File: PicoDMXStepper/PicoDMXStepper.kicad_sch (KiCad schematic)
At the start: 26 parts, among them J1 Pwr In, J2 DMX Serial, J3 Stepper Out, J4 Limit SW, SW2 SW_DIP_x04, U1 AMS1117-5.0, U2 Pico, U3 SP3485EN

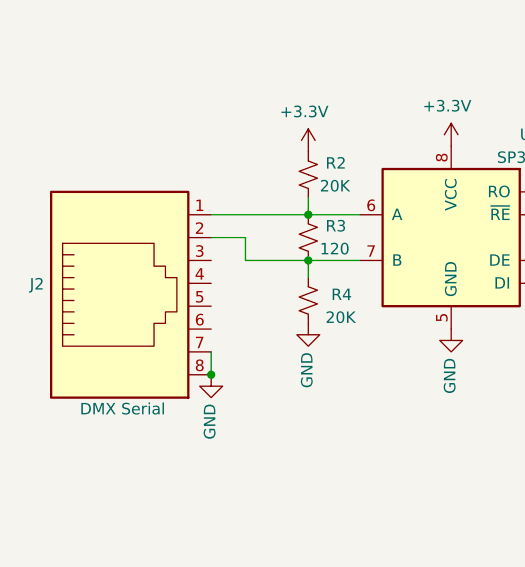
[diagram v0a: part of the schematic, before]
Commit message: Added untested Firmware and LCSC partnumbers
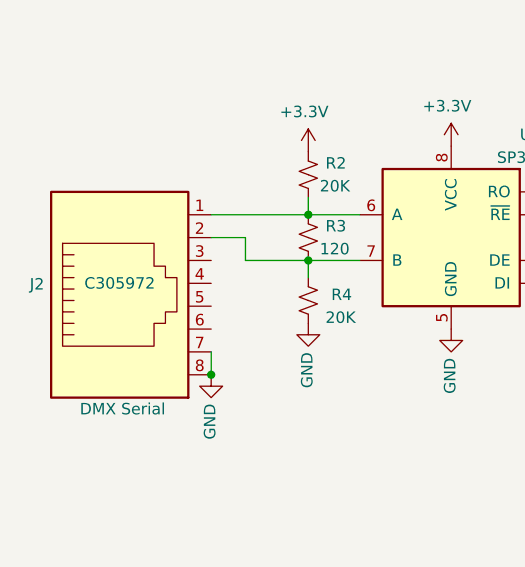
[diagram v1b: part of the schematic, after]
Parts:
- C1: LCSC (none) -> C445063
- C2: LCSC (none) -> C19702
- D1, R3: LCSC (none) -> C72043
- J1: LCSC (none) -> C306200
- J2: LCSC (none) -> C305972
- J3: LCSC (none) -> C192779
- J4: LCSC (none) -> C69809
- R1: LCSC (none) -> C23345
- R2, R4: LCSC (none) -> C4184
- R5, R6: LCSC (none) -> C25804
- SW2: LCSC (none) -> C509571
- U1: LCSC (none) -> C6187
- U3: LCSC (none) -> C8963
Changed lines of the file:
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@@
+      (effects (font (size 1.27 1.27)) hide)
+    )
+    (property "LCSC" "C306200" (at 55.626 49.657 0)
       (effects (font (size 1.27 1.27)) hide)
     )
@@
       (effects (font (size 1.27 1.27)) hide)
     )
+    (property "LCSC" "C445063" (at 80.4672 50.9016 0)
+      (effects (font (size 1.27 1.27)) hide)
+    )
     (pin "1")
     (pin "2")
@@
     )
     (property "Datasheet" "~" (at 104.14 52.07 0)
+      (effects (font (size 1.27 1.27)) hide)
+    )
+    (property "LCSC" "C19702" (at 107.1372 50.9016 0)
       (effects (font (size 1.27 1.27)) hide)
     )
@@
       (effects (font (size 1.27 1.27)) hide)
     )
-    (property "LCSC" "" (at 52.705 102.87 0)
+    (property "LCSC" "C305972" (at 52.705 102.87 0)
       (effects (font (size 1.27 1.27)))
     )
@@
       (effects (font (size 1.27 1.27)) hide)
     )
+    (property "LCSC" "C25804" (at 101.6 104.775 0)
+      (effects (font (size 1.27 1.27)) hide)
+    )
     (pin "1")
     (pin "2")
@@
       (effects (font (size 1.27 1.27)) hide)
     )
+    (property "LCSC" "C72043" (at 140.208 34.036 0)
+      (effects (font (size 1.27 1.27)) hide)
+    )
     (pin "1")
     (pin "2")
@@
     )
     (property "LCSC_PN" "C4184" (at 73.66 104.775 0)
+      (effects (font (size 1.27 1.27)) hide)
+    )
+    (property "LCSC" "C4184" (at 76.2 104.14 0)
       (effects (font (size 1.27 1.27)) hide)
     )
@@
     )
     (property "LCSC_PN" "C6187" (at 91.44 48.26 0)
+      (effects (font (size 1.27 1.27)) hide)
+    )
+    (property "LCSC" "C6187" (at 91.44 41.91 0)
       (effects (font (size 1.27 1.27)) hide)
     )
@@
       (effects (font (size 1.27 1.27)) hide)
     )
+    (property "LCSC" "C509571" (at 141.986 103.124 0)
+      (effects (font (size 1.27 1.27)) hide)
+    )
     (pin "1")
     (pin "2")
@@
       (effects (font (size 1.27 1.27)) hide)
     )
+    (property "LCSC" "C192779" (at 215.646 127.635 0)
+      (effects (font (size 1.27 1.27)) hide)
+    )
     (pin "1")
     (pin "2")
@@
       (effects (font (size 1.27 1.27)) hide)
     )
+    (property "LCSC" "C25804" (at 109.22 102.235 0)
+      (effects (font (size 1.27 1.27)) hide)
+    )
     (pin "1")
     (pin "2")
@@
     )
     (property "LCSC_PN" "C8963" (at 89.535 97.79 0)
+      (effects (font (size 1.27 1.27)) hide)
+    )
+    (property "LCSC" "C8963" (at 97.155 86.36 0)
       (effects (font (size 1.27 1.27)) hide)
     )
@@
       (effects (font (size 1.27 1.27)) hide)
     )
+    (property "LCSC" "C72043" (at 75.565 96.52 0)
+      (effects (font (size 1.27 1.27)) hide)
+    )
     (pin "1")
     (pin "2")
@@
       (effects (font (size 1.27 1.27)) hide)
     )
+    (property "LCSC" "C23345" (at 129.667 42.418 0)
+      (effects (font (size 1.27 1.27)) hide)
+    )
     (pin "1")
     (pin "2")
@@
     )
     (property "LCSC_PN" "C430599" (at 210.566 74.93 0)
+      (effects (font (size 1.27 1.27)) hide)
+    )
+    (property "LCSC" "C69809" (at 212.852 74.295 0)
       (effects (font (size 1.27 1.27)) hide)
     )
@@
       (effects (font (size 1.27 1.27)) hide)
     )
+    (property "LCSC" "C4184" (at 75.565 89.535 0)
+      (effects (font (size 1.27 1.27)) hide)
+    )

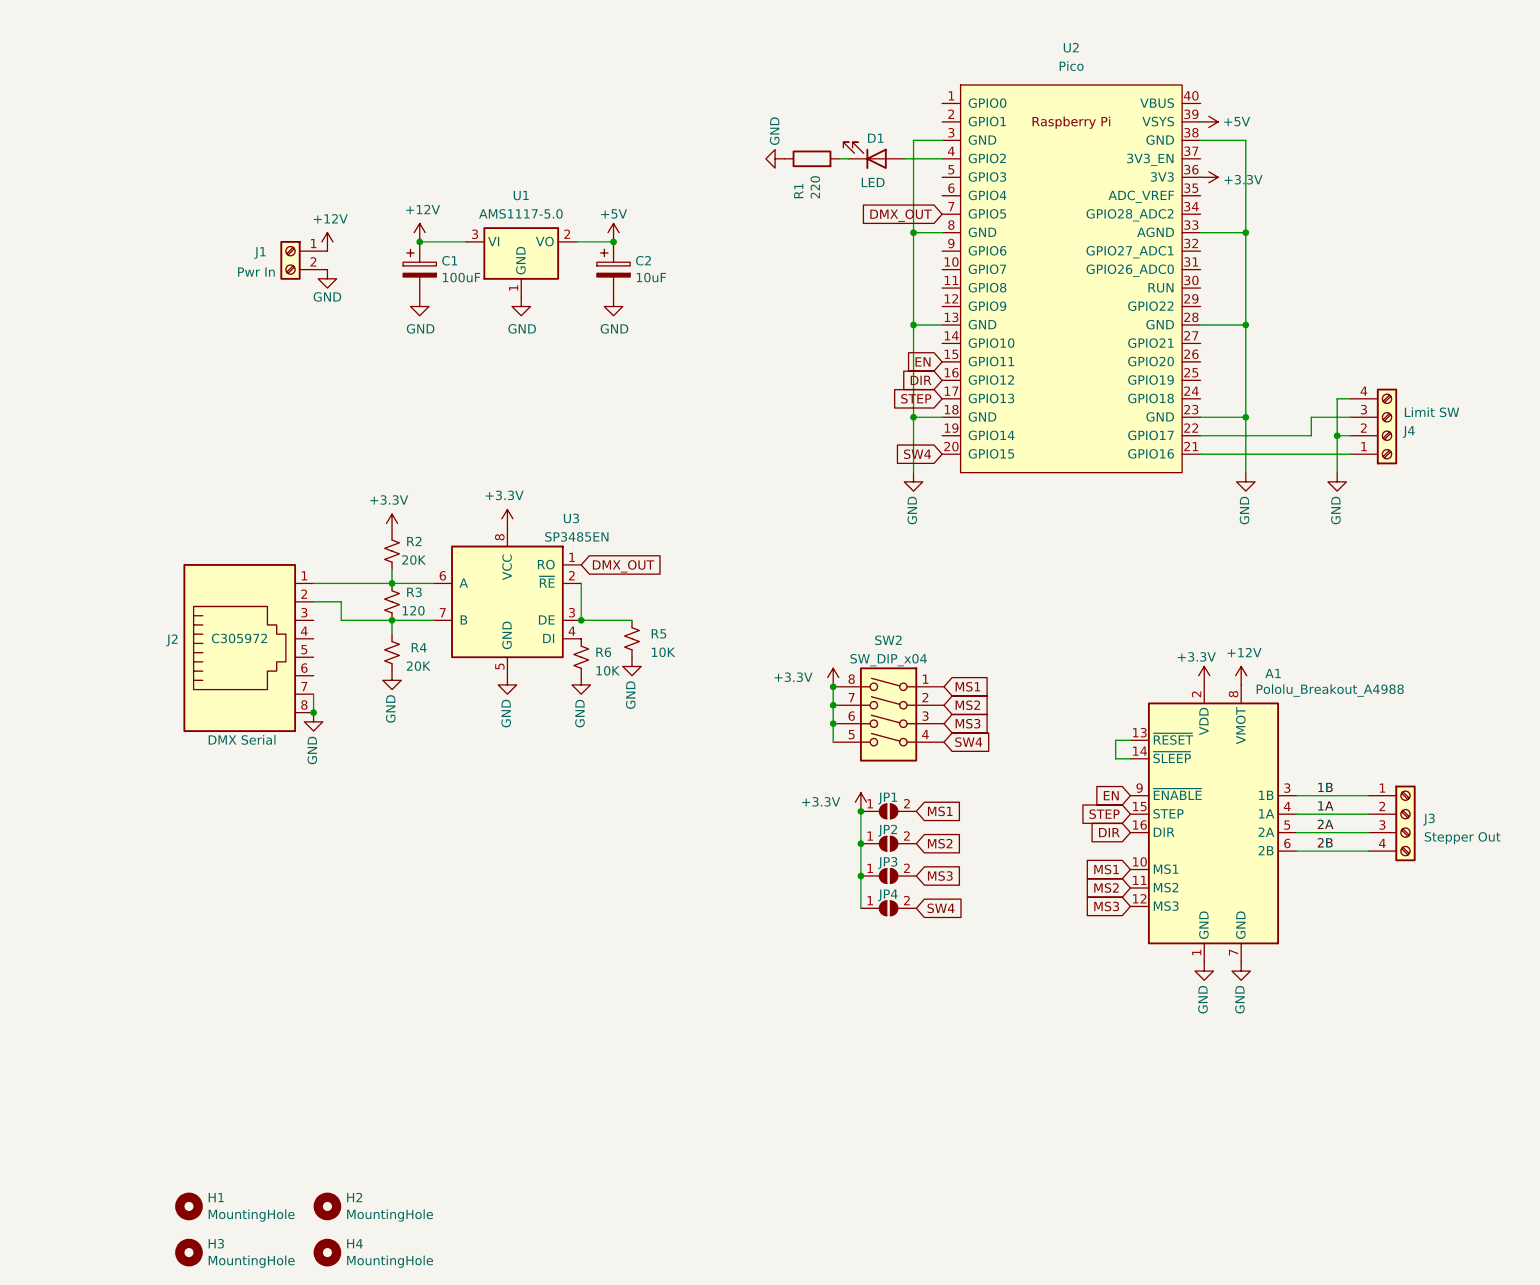
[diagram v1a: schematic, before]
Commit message: redo PCB layout, Add servo headers and opocouplers to limit switches
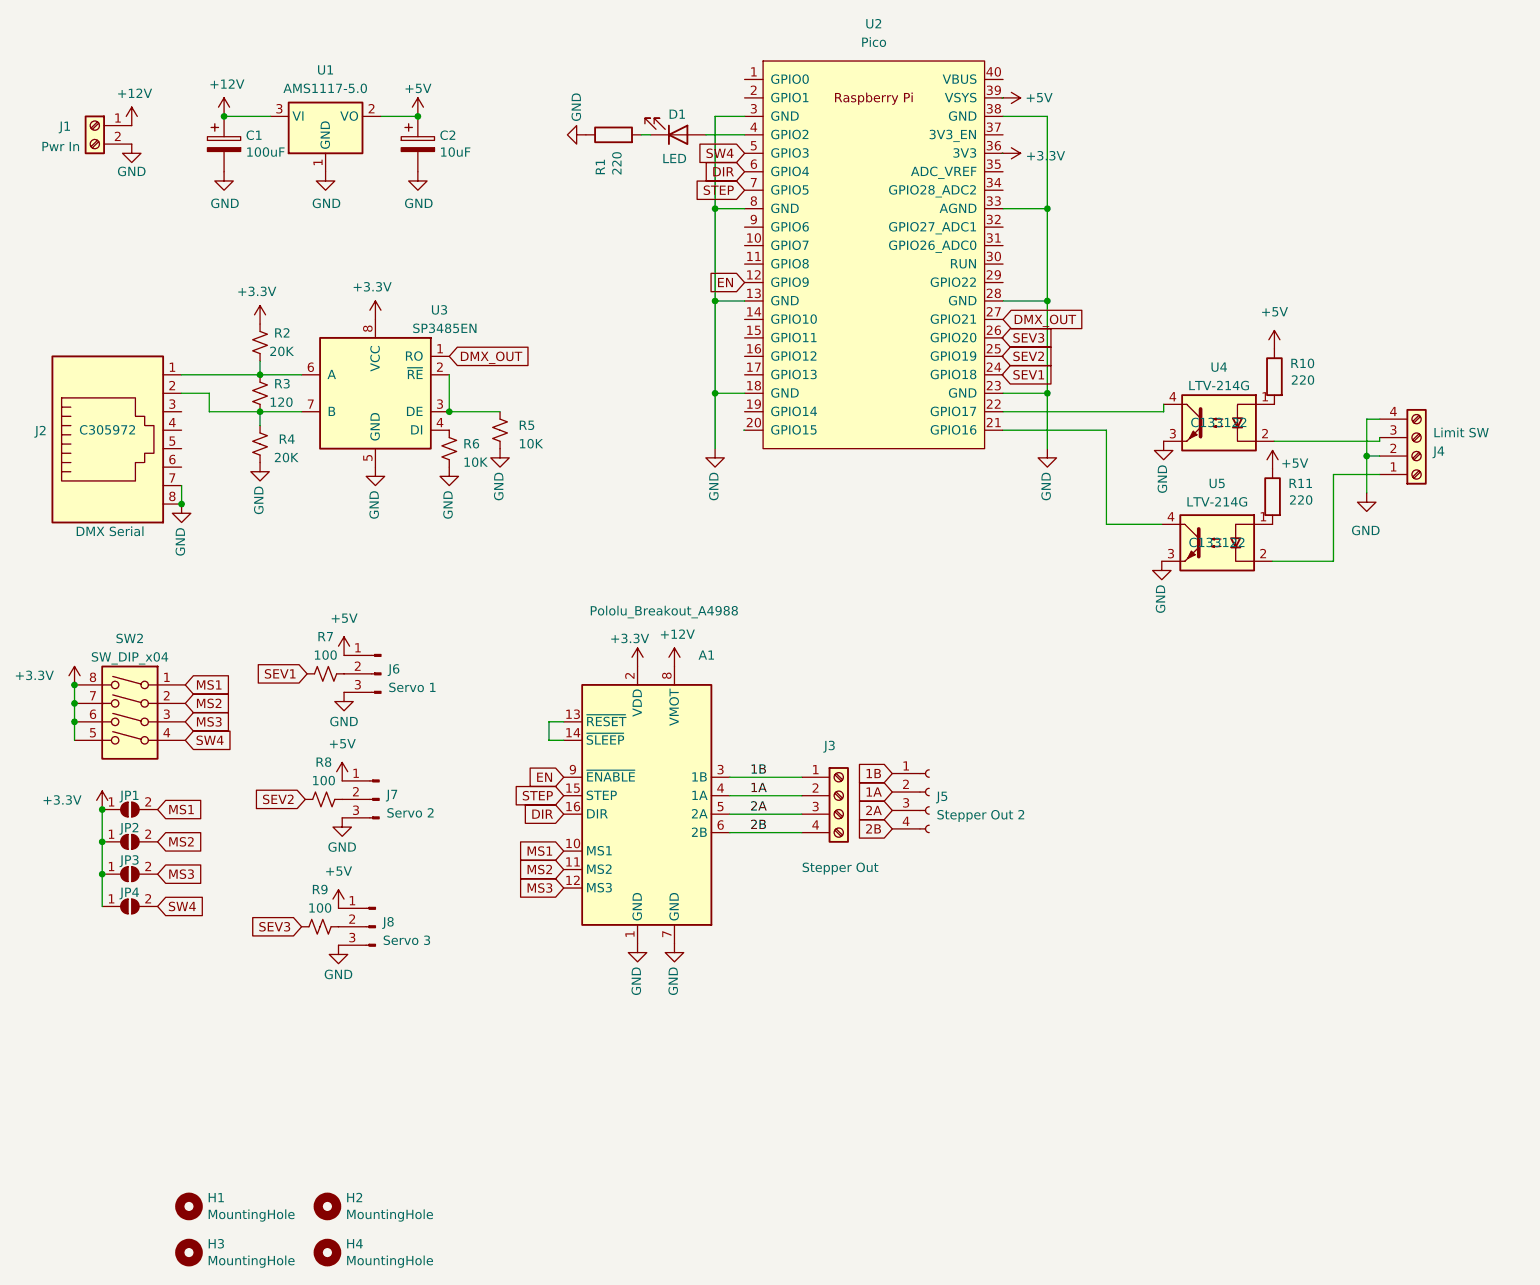
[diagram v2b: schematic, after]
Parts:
- added J5: Stepper Out 2, Connector_JST:JST_XH_B4B-XH-A_1x04_P2.50mm_Vertical, symbol Connector:Conn_01x04_Socket
- added J6: Servo 1, Connector_PinHeader_2.54mm:PinHeader_1x03_P2.54mm_Vertical, symbol Connector:Conn_01x03_Pin
- added J7: Servo 2, Connector_PinHeader_2.54mm:PinHeader_1x03_P2.54mm_Vertical, symbol Connector:Conn_01x03_Pin
- added J8: Servo 3, Connector_PinHeader_2.54mm:PinHeader_1x03_P2.54mm_Vertical, symbol Connector:Conn_01x03_Pin
- added R10, R11: 220, Resistor_SMD:R_0603_1608Metric_Pad0.98x0.95mm_HandSolder, symbol Device:R
- added R7, R8, R9: 100, Resistor_SMD:R_0603_1608Metric_Pad0.98x0.95mm_HandSolder, symbol Device:R_Small_US
- added U4, U5: LTV-214G, PicoDMXStepper:LTV214, symbol LTV-214:LTV-214G
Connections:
- net +5V: now also J6.1 (Pin_1), J7.1 (Pin_1), J8.1 (Pin_1), R10.1, R11.1
- net 1A: now also J5.2 (Pin_2)
- net 1B: now also J5.1 (Pin_1)
- net 2A: now also J5.3 (Pin_3)
- net 2B: now also J5.4 (Pin_4)
- net DIR: now also U2.6 (GPIO4); no longer U2.16 (GPIO12)
- net DMX_OUT: now also U2.27 (GPIO21); no longer U2.7 (GPIO5)
- net EN: now also U2.12 (GPIO9); no longer U2.15 (GPIO11)
- net GND: now also J6.3 (Pin_3), J7.3 (Pin_3), J8.3 (Pin_3), U4.3, U5.3
- net STEP: now also U2.7 (GPIO5); no longer U2.17 (GPIO13)
- net SW4: now also U2.5 (GPIO3); no longer U2.20 (GPIO15)
- net at J4.1 (Pin_1): now also U5.2; no longer U2.21 (GPIO16)
- net at J4.3 (Pin_3): now also U4.2; no longer U2.22 (GPIO17)
- net SEV1: now reaches U2.24 (GPIO18)
- net SEV1: now also R7.1
- net SEV2: now reaches U2.25 (GPIO19)
- net SEV2: now also R8.1
- net SEV3: now reaches U2.26 (GPIO20)
- net SEV3: now also R9.1
- new net: J6.2 (Pin_2), R7.2
- new net: R11.2, U5.1
- new net: U2.21 (GPIO16), U5.4
- new net: R10.2, U4.1
- new net: U2.22 (GPIO17), U4.4
- new net: J8.2 (Pin_2), R9.2
- new net: J7.2 (Pin_2), R8.2
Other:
- moved on the sheet: A1, C1, C2, D1, J1, J2, J3, J4, JP1, JP2, JP3, JP4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

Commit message: added Optocoupler to limits switches
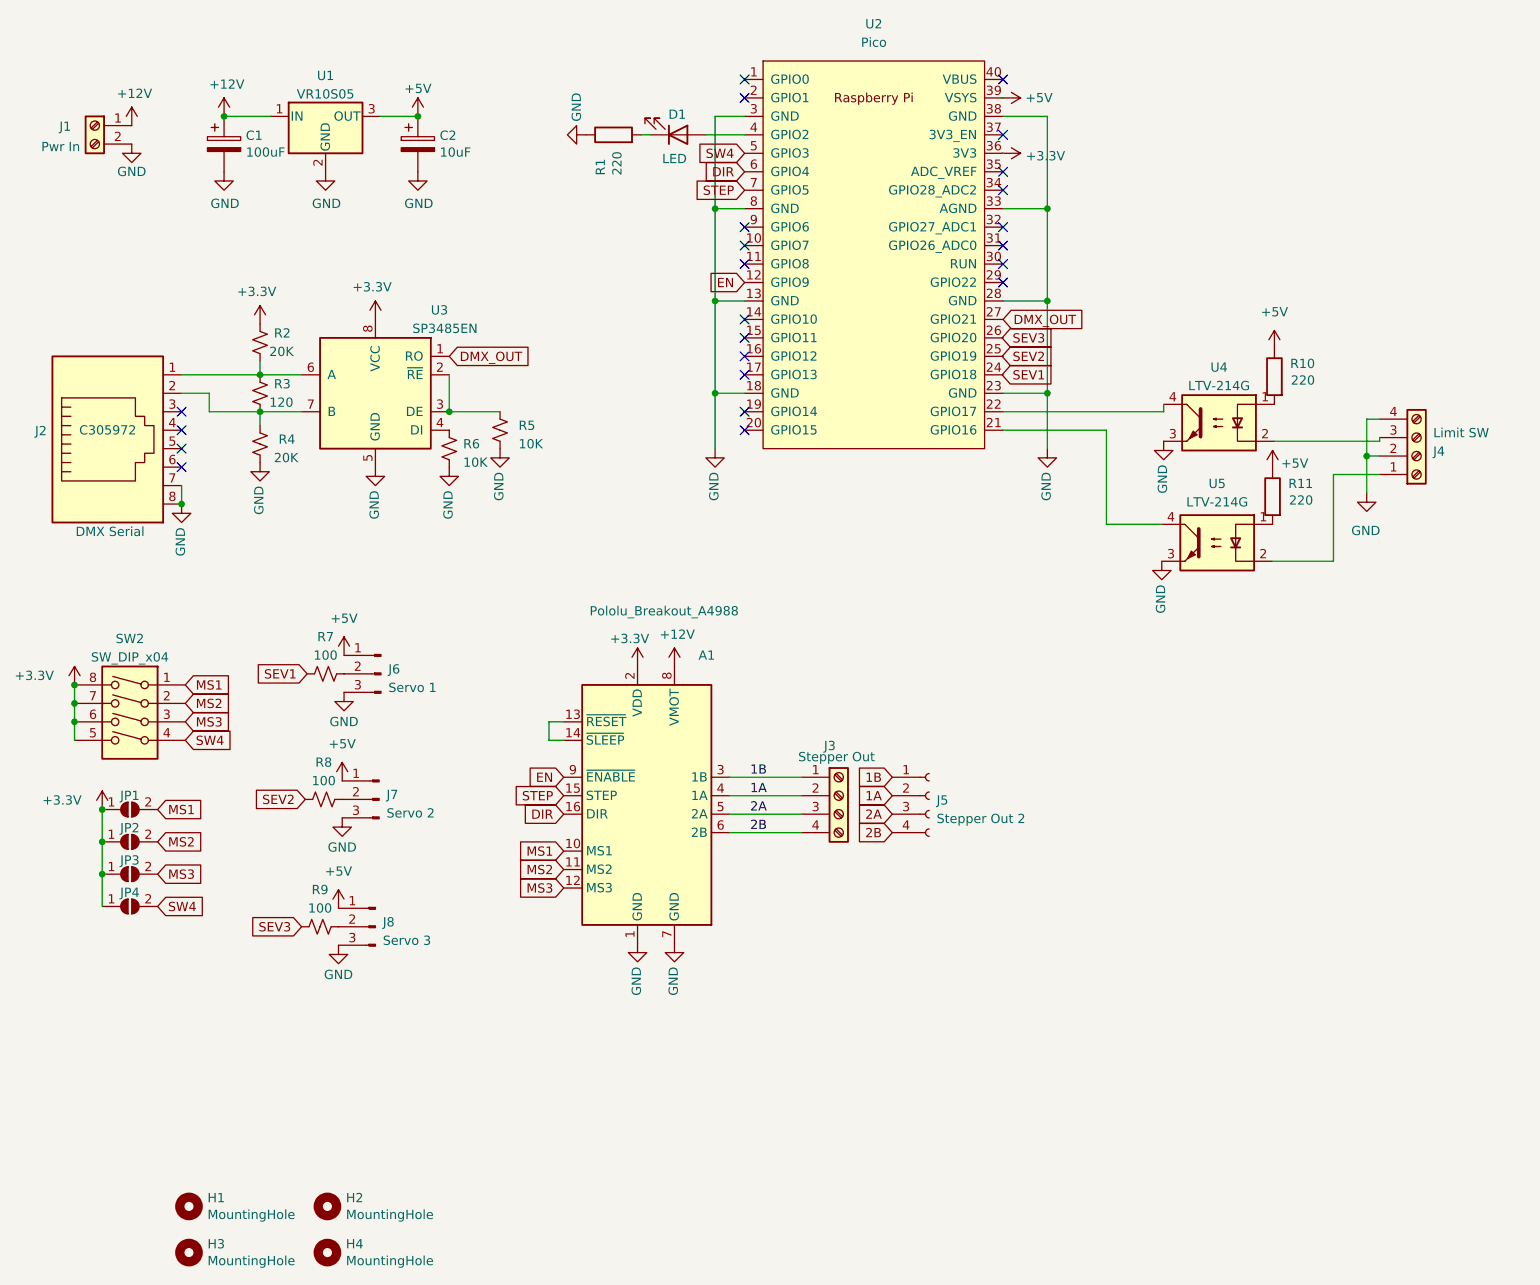
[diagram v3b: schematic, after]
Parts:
- removed U1: AMS1117-5.0, Package_TO_SOT_SMD:SOT-223-3_TabPin2, symbol Regulator_Linear:AMS1117-5.0
- added U1: VR10S05, PicoDMXStepper:VR10S05, symbol Regulator_Linear:L7805
- H1, H2, H3, H4, JP1, JP2, JP3, JP4: now left out of the parts list
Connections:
- net +12V: now also U1.1 (IN)
- net +5V: now also U1.3 (OUT)
- net GND: now also U1.2 (GND)
- no-connect marks 0 -> 23
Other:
- moved on the sheet: J5

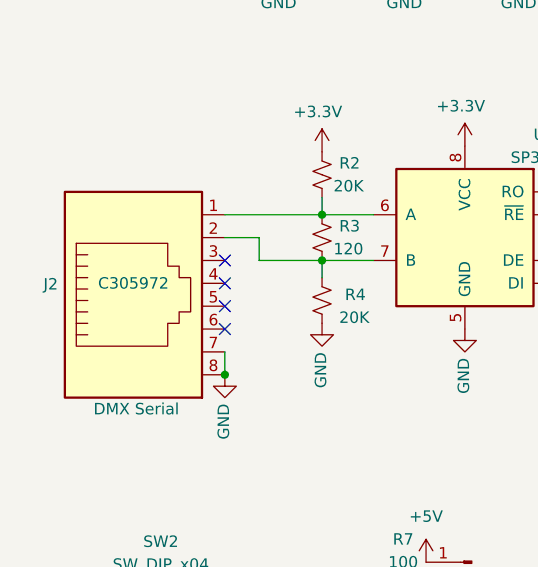
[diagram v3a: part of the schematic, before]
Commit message: fix RJ45 LCSC PN
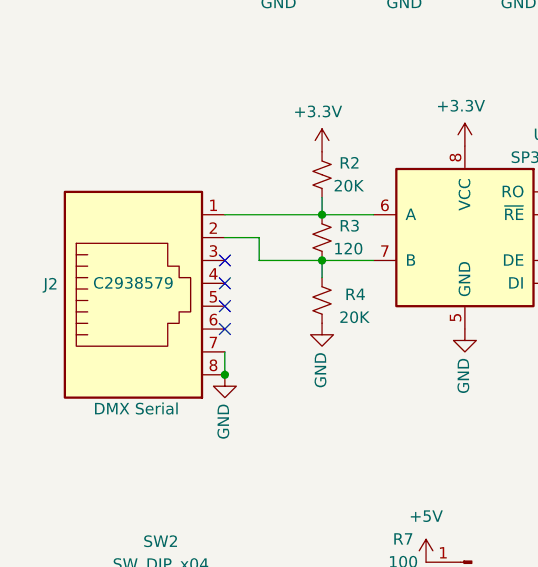
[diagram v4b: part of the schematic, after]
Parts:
- J2: LCSC C305972 -> C2938579
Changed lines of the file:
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@@
       (effects (font (size 1.27 1.27)) hide)
     )
-    (property "LCSC" "C305972" (at 34.544 74.168 0)
+    (property "LCSC" "C2938579" (at 34.544 74.168 0)
       (effects (font (size 1.27 1.27)))
     )
